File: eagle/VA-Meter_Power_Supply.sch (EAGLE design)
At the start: 18 parts, among them IC2 7805TV, T1 2SA1359

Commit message: Power Supply 回路図、基板図修正
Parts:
- JP1: device pinhead:PINHD-1X3 -> pinhead:PINHD-2X3
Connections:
- net 3.3V: now also JP1.3, JP1.4; no longer JP1.2
- net 5V: now also JP1.2
- net V-GND: now also JP1.5, JP1.6; no longer JP1.3
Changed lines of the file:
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@@
 <setting verticaltext="up"/>
 </settings>
-<grid distance="0.1" unitdist="inch" unit="inch" style="dots" multiple="1" display="yes" altdistance="0.01" altunitdist="inch" altunit="inch"/>
+<grid distance="0.1" unitdist="inch" unit="inch" style="lines" multiple="1" display="yes" altdistance="0.01" altunitdist="inch" altunit="inch"/>
 <layers>
 <layer number="1" name="Top" color="4" fill="1" visible="no" active="no"/>
@@
 <part name="PF1" library="polyswitch" deviceset="PTC-" device="PF-5.1"/>
 <part name="FRAME1" library="frames" deviceset="A4L-LOC" device=""/>
-<part name="JP1" library="pinhead" deviceset="PINHD-1X3" device=""/>
+<part name="JP1" library="pinhead" deviceset="PINHD-2X3" device=""/>
 </parts>
 <sheets>
@@
 <wire x1="121.92" y1="60.96" x2="137.16" y2="60.96" width="0.1524" layer="91"/>
 <label x="127" y="60.96" size="1.778" layer="95"/>
+<wire x1="121.92" y1="71.12" x2="149.86" y2="71.12" width="0.1524" layer="91"/>
+<wire x1="149.86" y1="71.12" x2="149.86" y2="60.96" width="0.1524" layer="91"/>
+<junction x="121.92" y="71.12"/>
+<pinref part="JP1" gate="A" pin="2"/>
+<wire x1="149.86" y1="60.96" x2="144.78" y2="60.96" width="0.1524" layer="91"/>
 </segment>
 </net>
@@
 <wire x1="111.76" y1="48.26" x2="111.76" y2="45.72" width="0.1524" layer="91"/>
 <wire x1="99.06" y1="45.72" x2="111.76" y2="45.72" width="0.1524" layer="91"/>
-<pinref part="JP1" gate="A" pin="3"/>
+<pinref part="JP1" gate="A" pin="5"/>
 <wire x1="137.16" y1="55.88" x2="121.92" y2="55.88" width="0.1524" layer="91"/>
 <wire x1="121.92" y1="55.88" x2="121.92" y2="45.72" width="0.1524" layer="91"/>
@@
 <junction x="111.76" y="45.72"/>
 <label x="127" y="53.34" size="1.778" layer="95"/>
+<wire x1="121.92" y1="45.72" x2="149.86" y2="45.72" width="0.1524" layer="91"/>
+<junction x="121.92" y="45.72"/>
+<wire x1="149.86" y1="45.72" x2="149.86" y2="55.88" width="0.1524" layer="91"/>
+<pinref part="JP1" gate="A" pin="6"/>
+<wire x1="149.86" y1="55.88" x2="144.78" y2="55.88" width="0.1524" layer="91"/>
 </segment>
 </net>
@@
 <wire x1="111.76" y1="60.96" x2="111.76" y2="58.42" width="0.1524" layer="91"/>
 <wire x1="111.76" y1="58.42" x2="111.76" y2="53.34" width="0.1524" layer="91"/>
-<wire x1="137.16" y1="58.42" x2="111.76" y2="58.42" width="0.1524" layer="91"/>
+<wire x1="137.16" y1="58.42" x2="129.54" y2="58.42" width="0.1524" layer="91"/>
 <junction x="111.76" y="58.42"/>
-<pinref part="JP1" gate="A" pin="2"/>
+<pinref part="JP1" gate="A" pin="3"/>
 <label x="127" y="58.42" size="1.778" layer="95"/>
-</segment>
-</net>
+<wire x1="129.54" y1="58.42" x2="111.76" y2="58.42" width="0.1524" layer="91"/>
+<wire x1="129.54" y1="58.42" x2="129.54" y2="48.26" width="0.1524" layer="91"/>
+<junction x="129.54" y="58.42"/>
+<wire x1="129.54" y1="48.26" x2="152.4" y2="48.26" width="0.1524" layer="91"/>
+<wire x1="152.4" y1="48.26" x2="152.4" y2="58.42" width="0.1524" layer="91"/>
+<pinref part="JP1" gate="A" pin="4"/>
+<wire x1="152.4" y1="58.42" x2="144.78" y2="58.42" width="0.1524" layer="91"/>
+</segment>
+</net>

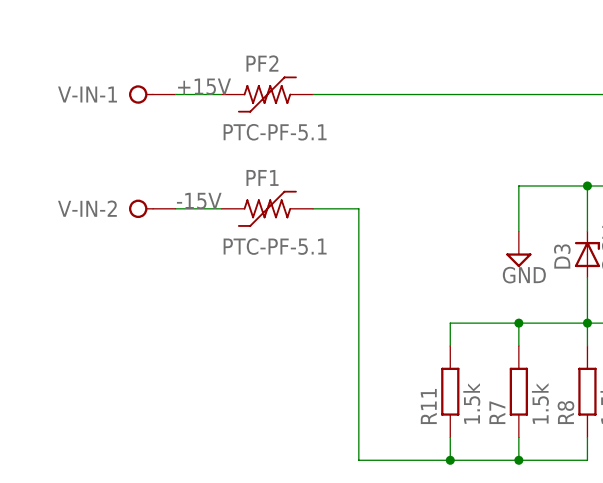
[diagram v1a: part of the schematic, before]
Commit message: VA-Meter_Power_Supply 測定部電源の回路図、基板図修正 入力端子にGNDを追加
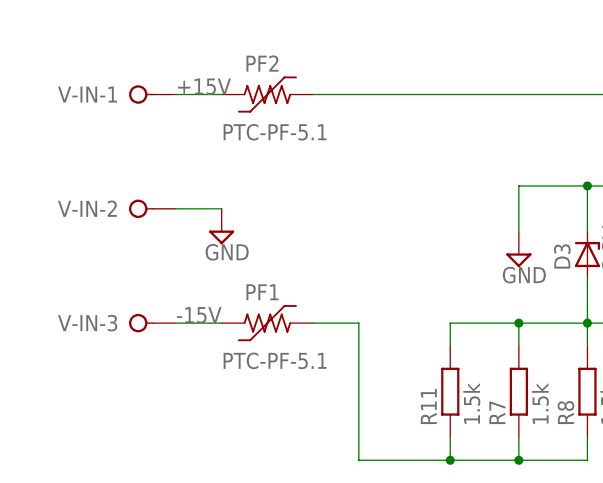
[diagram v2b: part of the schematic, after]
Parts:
- V-IN: device con-wago-508:W237-02P -> con-wago-508:W237-03P
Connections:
- net GND: now also V-IN-2.KL
- net N$7: now also V-IN-3.KL; no longer V-IN-2.KL
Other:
- moved on the sheet: PF1
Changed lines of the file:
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@@
 <setting verticaltext="up"/>
 </settings>
-<grid distance="0.1" unitdist="inch" unit="inch" style="lines" multiple="1" display="yes" altdistance="0.01" altunitdist="inch" altunit="inch"/>
+<grid distance="0.1" unitdist="inch" unit="inch" style="lines" multiple="1" display="no" altdistance="0.01" altunitdist="inch" altunit="inch"/>
 <layers>
 <layer number="1" name="Top" color="4" fill="1" visible="no" active="no"/>
@@
 <part name="C2" library="rcl" deviceset="CPOL-EU" device="E2.5-5" value="10u"/>
 <part name="C3" library="rcl" deviceset="CPOL-EU" device="E2.5-6" value="100u"/>
-<part name="V-IN" library="con-wago-508" deviceset="W237-02P" device=""/>
 <part name="D1" library="diode" deviceset="SCHOTTKY-DIODE" device="DO35-7" value="1S2"/>
 <part name="D2" library="diode" deviceset="ZENER-DIODE" device="ZD-5" value="3.6V"/>
@@
 <part name="FRAME1" library="frames" deviceset="A4L-LOC" device=""/>
 <part name="JP1" library="pinhead" deviceset="PINHD-2X3" device=""/>
+<part name="V-IN" library="con-wago-508" deviceset="W237-03P" device=""/>
+<part name="SUPPLY1" library="supply2" deviceset="GND" device=""/>
 </parts>
 <sheets>
@@
 <instance part="C2" gate="G$1" x="53.34" y="58.42"/>
 <instance part="C3" gate="G$1" x="99.06" y="58.42"/>
-<instance part="V-IN" gate="-1" x="-20.32" y="71.12"/>
-<instance part="V-IN" gate="-2" x="-20.32" y="58.42"/>
 <instance part="D1" gate="G$1" x="76.2" y="83.82" rot="R180"/>
 <instance part="D2" gate="G$1" x="111.76" y="50.8" rot="R90"/>
@@
 <instance part="R11" gate="G$1" x="15.24" y="38.1" rot="R90"/>
 <instance part="PF2" gate="G$1" x="-5.08" y="71.12"/>
-<instance part="PF1" gate="G$1" x="-5.08" y="58.42"/>
+<instance part="PF1" gate="G$1" x="-5.08" y="45.72"/>
 <instance part="FRAME1" gate="G$1" x="-55.88" y="-30.48"/>
 <instance part="JP1" gate="A" x="139.7" y="58.42"/>
+<instance part="V-IN" gate="-1" x="-20.32" y="71.12"/>
+<instance part="V-IN" gate="-2" x="-20.32" y="58.42"/>
+<instance part="V-IN" gate="-3" x="-20.32" y="45.72"/>
+<instance part="SUPPLY1" gate="GND" x="-10.16" y="55.88"/>
 </instances>
 <busses>
@@
 <wire x1="22.86" y1="60.96" x2="30.48" y2="60.96" width="0.1524" layer="91"/>
 <junction x="30.48" y="60.96"/>
+</segment>
+<segment>
+<pinref part="V-IN" gate="-2" pin="KL"/>
+<pinref part="SUPPLY1" gate="GND" pin="GND"/>
+<wire x1="-10.16" y1="58.42" x2="-15.24" y2="58.42" width="0.1524" layer="91"/>
 </segment>
 </net>
@@
 <net name="-15V" class="0">
 <segment>
-<label x="-15.24" y="58.42" size="1.778" layer="95"/>
+<label x="-15.24" y="45.72" size="1.778" layer="95"/>
 <pinref part="R8" gate="G$1" pin="1"/>
 <wire x1="30.48" y1="33.02" x2="30.48" y2="30.48" width="0.1524" layer="91"/>
@@
 <wire x1="15.24" y1="30.48" x2="5.08" y2="30.48" width="0.1524" layer="91"/>
 <junction x="15.24" y="30.48"/>
-<wire x1="5.08" y1="30.48" x2="5.08" y2="58.42" width="0.1524" layer="91"/>
+<wire x1="5.08" y1="30.48" x2="5.08" y2="45.72" width="0.1524" layer="91"/>
 <pinref part="PF1" gate="G$1" pin="2"/>
-<wire x1="0" y1="58.42" x2="5.08" y2="58.42" width="0.1524" layer="91"/>
+<wire x1="0" y1="45.72" x2="5.08" y2="45.72" width="0.1524" layer="91"/>
 </segment>
 </net>
@@
 <net name="N$6" class="0">
 <segment>
-<pinref part="V-IN" gate="-1" pin="KL"/>
 <pinref part="PF2" gate="G$1" pin="1"/>
 <wire x1="-15.24" y1="71.12" x2="-10.16" y2="71.12" width="0.1524" layer="91"/>
+<pinref part="V-IN" gate="-1" pin="KL"/>
 </segment>
 </net>
 <net name="N$7" class="0">
 <segment>
-<pinref part="V-IN" gate="-2" pin="KL"/>
 <pinref part="PF1" gate="G$1" pin="1"/>
-<wire x1="-15.24" y1="58.42" x2="-10.16" y2="58.42" width="0.1524" layer="91"/>
-</segment>
-</net>
+<wire x1="-15.24" y1="45.72" x2="-10.16" y2="45.72" width="0.1524" layer="91"/>
+<pinref part="V-IN" gate="-3" pin="KL"/>
+</segment>
+</net>

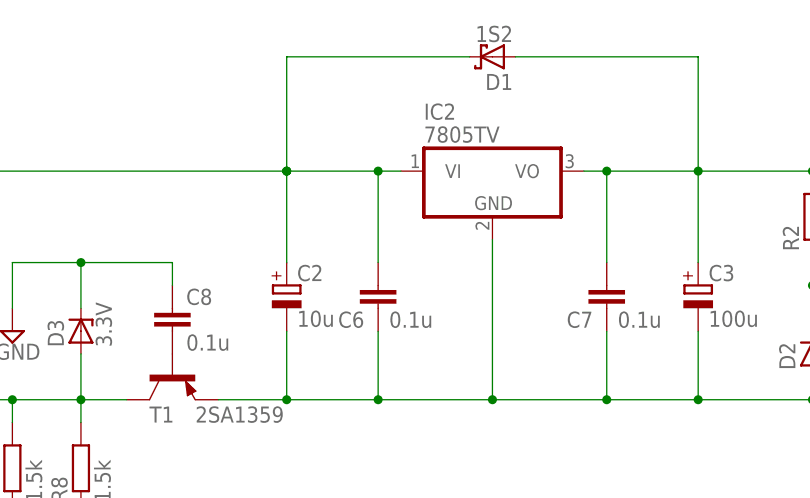
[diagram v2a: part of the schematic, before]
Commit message: VA-Meter_Power_Supply 回路図の電解コンデンサの値を47uFに変更
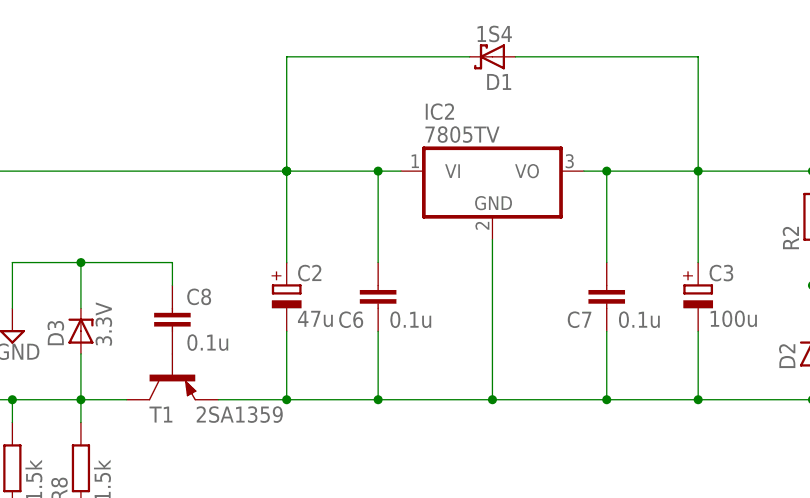
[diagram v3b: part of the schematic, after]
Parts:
- C2: value 10u -> 47u
- D1: value 1S2 -> 1S4
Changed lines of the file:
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@@
 <part name="R8" library="rcl" deviceset="R-EU_" device="0207/7" value="1.5k"/>
 <part name="SUPPLY4" library="supply2" deviceset="GND" device=""/>
-<part name="C2" library="rcl" deviceset="CPOL-EU" device="E2.5-5" value="10u"/>
+<part name="C2" library="rcl" deviceset="CPOL-EU" device="E2.5-5" value="47u"/>
 <part name="C3" library="rcl" deviceset="CPOL-EU" device="E2.5-6" value="100u"/>
-<part name="D1" library="diode" deviceset="SCHOTTKY-DIODE" device="DO35-7" value="1S2"/>
+<part name="D1" library="diode" deviceset="SCHOTTKY-DIODE" device="DO35-7" value="1S4"/>
 <part name="D2" library="diode" deviceset="ZENER-DIODE" device="ZD-5" value="3.6V"/>
 <part name="R2" library="rcl" deviceset="R-EU_" device="0204/7" value="220"/>

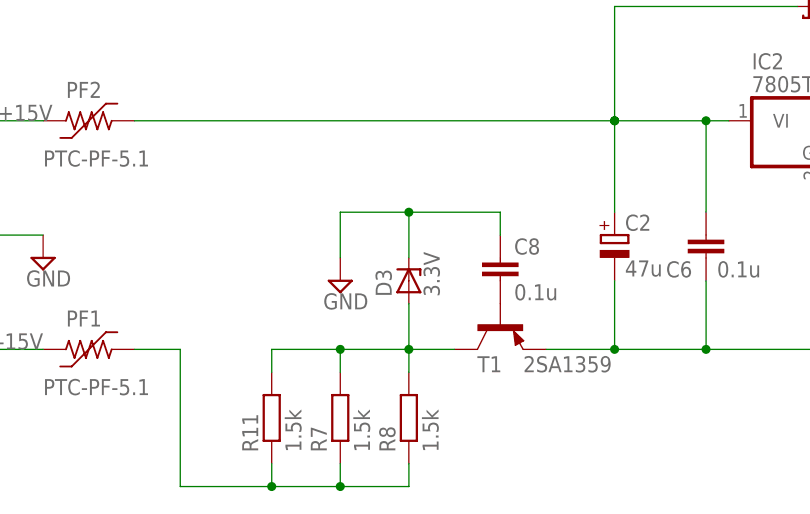
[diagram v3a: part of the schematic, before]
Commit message: VA-Meter_Power_Supply 2SA1359の定電圧源の回路が間違っていたので修正
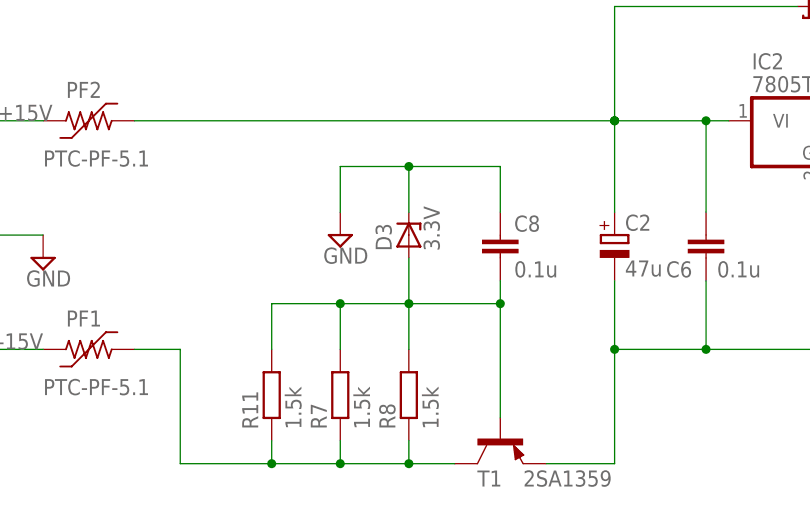
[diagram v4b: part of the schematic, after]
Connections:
- removed net N$1: D3.A, R11.2, R7.2, R8.2, T1.C
- removed net N$5: C8.2, T1.B
- new net N$2: C8.2, D3.A, R11.2, R7.2, R8.2, T1.B
- net -15V: now also T1.C
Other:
- moved on the sheet: C8, D3, R11, R7, R8, T1
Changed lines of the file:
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@@
 <instances>
 <instance part="IC2" gate="A1" x="76.2" y="71.12"/>
-<instance part="R8" gate="G$1" x="30.48" y="38.1" rot="R90"/>
-<instance part="SUPPLY4" gate="GND" x="22.86" y="53.34"/>
+<instance part="R8" gate="G$1" x="30.48" y="40.64" rot="R90"/>
+<instance part="SUPPLY4" gate="GND" x="22.86" y="58.42"/>
 <instance part="C2" gate="G$1" x="53.34" y="58.42"/>
 <instance part="C3" gate="G$1" x="99.06" y="58.42"/>
@@
 <attribute name="VALUE" x="94.996" y="55.499" size="1.778" layer="96" rot="R180"/>
 </instance>
-<instance part="D3" gate="G$1" x="30.48" y="53.34" rot="R90"/>
-<instance part="C8" gate="G$1" x="40.64" y="55.88"/>
-<instance part="T1" gate="G$1" x="40.64" y="48.26" smashed="yes" rot="R270">
-<attribute name="NAME" x="38.1" y="43.18" size="1.778" layer="95"/>
-<attribute name="VALUE" x="43.18" y="43.18" size="1.778" layer="96"/>
+<instance part="D3" gate="G$1" x="30.48" y="58.42" rot="R90"/>
+<instance part="C8" gate="G$1" x="40.64" y="58.42"/>
+<instance part="T1" gate="G$1" x="40.64" y="35.56" smashed="yes" rot="R270">
+<attribute name="NAME" x="38.1" y="30.48" size="1.778" layer="95"/>
+<attribute name="VALUE" x="43.18" y="30.48" size="1.778" layer="96"/>
 </instance>
-<instance part="R7" gate="G$1" x="22.86" y="38.1" rot="R90"/>
-<instance part="R11" gate="G$1" x="15.24" y="38.1" rot="R90"/>
+<instance part="R7" gate="G$1" x="22.86" y="40.64" rot="R90"/>
+<instance part="R11" gate="G$1" x="15.24" y="40.64" rot="R90"/>
 <instance part="PF2" gate="G$1" x="-5.08" y="71.12"/>
 <instance part="PF1" gate="G$1" x="-5.08" y="45.72"/>
@@
 <segment>
 <pinref part="SUPPLY4" gate="GND" pin="GND"/>
-<wire x1="22.86" y1="55.88" x2="22.86" y2="60.96" width="0.1524" layer="91"/>
+<wire x1="22.86" y1="60.96" x2="22.86" y2="66.04" width="0.1524" layer="91"/>
 <pinref part="D3" gate="G$1" pin="C"/>
-<wire x1="30.48" y1="60.96" x2="30.48" y2="55.88" width="0.1524" layer="91"/>
-<wire x1="30.48" y1="60.96" x2="40.64" y2="60.96" width="0.1524" layer="91"/>
+<wire x1="30.48" y1="66.04" x2="30.48" y2="60.96" width="0.1524" layer="91"/>
+<wire x1="30.48" y1="66.04" x2="40.64" y2="66.04" width="0.1524" layer="91"/>
 <pinref part="C8" gate="G$1" pin="1"/>
-<wire x1="40.64" y1="60.96" x2="40.64" y2="58.42" width="0.1524" layer="91"/>
-<wire x1="22.86" y1="60.96" x2="30.48" y2="60.96" width="0.1524" layer="91"/>
-<junction x="30.48" y="60.96"/>
+<wire x1="40.64" y1="66.04" x2="40.64" y2="60.96" width="0.1524" layer="91"/>
+<wire x1="22.86" y1="66.04" x2="30.48" y2="66.04" width="0.1524" layer="91"/>
+<junction x="30.48" y="66.04"/>
 </segment>
 <segment>
@@
 <label x="-15.24" y="45.72" size="1.778" layer="95"/>
 <pinref part="R8" gate="G$1" pin="1"/>
-<wire x1="30.48" y1="33.02" x2="30.48" y2="30.48" width="0.1524" layer="91"/>
+<wire x1="30.48" y1="35.56" x2="30.48" y2="33.02" width="0.1524" layer="91"/>
 <pinref part="R11" gate="G$1" pin="1"/>
-<wire x1="15.24" y1="33.02" x2="15.24" y2="30.48" width="0.1524" layer="91"/>
-<wire x1="15.24" y1="30.48" x2="22.86" y2="30.48" width="0.1524" layer="91"/>
+<wire x1="15.24" y1="35.56" x2="15.24" y2="33.02" width="0.1524" layer="91"/>
+<wire x1="15.24" y1="33.02" x2="22.86" y2="33.02" width="0.1524" layer="91"/>
 <pinref part="R7" gate="G$1" pin="1"/>
-<wire x1="22.86" y1="30.48" x2="30.48" y2="30.48" width="0.1524" layer="91"/>
-<wire x1="22.86" y1="33.02" x2="22.86" y2="30.48" width="0.1524" layer="91"/>
-<junction x="22.86" y="30.48"/>
-<wire x1="15.24" y1="30.48" x2="5.08" y2="30.48" width="0.1524" layer="91"/>
-<junction x="15.24" y="30.48"/>
-<wire x1="5.08" y1="30.48" x2="5.08" y2="45.72" width="0.1524" layer="91"/>
+<wire x1="22.86" y1="33.02" x2="30.48" y2="33.02" width="0.1524" layer="91"/>
+<wire x1="22.86" y1="35.56" x2="22.86" y2="33.02" width="0.1524" layer="91"/>
+<junction x="22.86" y="33.02"/>
+<wire x1="15.24" y1="33.02" x2="5.08" y2="33.02" width="0.1524" layer="91"/>
+<junction x="15.24" y="33.02"/>
+<wire x1="5.08" y1="33.02" x2="5.08" y2="45.72" width="0.1524" layer="91"/>
 <pinref part="PF1" gate="G$1" pin="2"/>
 <wire x1="0" y1="45.72" x2="5.08" y2="45.72" width="0.1524" layer="91"/>
-</segment>
-</net>
-<net name="N$1" class="0">
-<segment>
-<pinref part="R8" gate="G$1" pin="2"/>
-<pinref part="D3" gate="G$1" pin="A"/>
-<wire x1="30.48" y1="50.8" x2="30.48" y2="45.72" width="0.1524" layer="91"/>
+<wire x1="30.48" y1="33.02" x2="35.56" y2="33.02" width="0.1524" layer="91"/>
+<junction x="30.48" y="33.02"/>
 <pinref part="T1" gate="G$1" pin="C"/>
-<wire x1="30.48" y1="45.72" x2="30.48" y2="43.18" width="0.1524" layer="91"/>
-<wire x1="35.56" y1="45.72" x2="30.48" y2="45.72" width="0.1524" layer="91"/>
-<junction x="30.48" y="45.72"/>
-<wire x1="30.48" y1="45.72" x2="22.86" y2="45.72" width="0.1524" layer="91"/>
-<pinref part="R11" gate="G$1" pin="2"/>
-<wire x1="22.86" y1="45.72" x2="15.24" y2="45.72" width="0.1524" layer="91"/>
-<wire x1="15.24" y1="45.72" x2="15.24" y2="43.18" width="0.1524" layer="91"/>
-<pinref part="R7" gate="G$1" pin="2"/>
-<wire x1="22.86" y1="43.18" x2="22.86" y2="45.72" width="0.1524" layer="91"/>
-<junction x="22.86" y="45.72"/>
-</segment>
-</net>
-<net name="N$5" class="0">
-<segment>
-<pinref part="T1" gate="G$1" pin="B"/>
-<pinref part="C8" gate="G$1" pin="2"/>
 </segment>
 </net>
@@
 <wire x1="88.9" y1="53.34" x2="88.9" y2="45.72" width="0.1524" layer="91"/>
 <junction x="88.9" y="45.72"/>
-<pinref part="T1" gate="G$1" pin="E"/>
-<wire x1="45.72" y1="45.72" x2="53.34" y2="45.72" width="0.1524" layer="91"/>
-<junction x="53.34" y="45.72"/>
 <pinref part="D2" gate="G$1" pin="A"/>
 <wire x1="111.76" y1="48.26" x2="111.76" y2="45.72" width="0.1524" layer="91"/>
@@
 <pinref part="JP1" gate="A" pin="6"/>
 <wire x1="149.86" y1="55.88" x2="144.78" y2="55.88" width="0.1524" layer="91"/>
+<pinref part="T1" gate="G$1" pin="E"/>
+<wire x1="53.34" y1="33.02" x2="45.72" y2="33.02" width="0.1524" layer="91"/>
+<wire x1="53.34" y1="33.02" x2="53.34" y2="45.72" width="0.1524" layer="91"/>
+<junction x="53.34" y="45.72"/>
 </segment>
 </net>
@@
 </segment>
 </net>
+<net name="N$2" class="0">
+<segment>
+<pinref part="R7" gate="G$1" pin="2"/>
+<pinref part="R8" gate="G$1" pin="2"/>
+<pinref part="D3" gate="G$1" pin="A"/>
+<wire x1="30.48" y1="55.88" x2="30.48" y2="50.8" width="0.1524" layer="91"/>
+<wire x1="30.48" y1="50.8" x2="30.48" y2="45.72" width="0.1524" layer="91"/>
+<pinref part="T1" gate="G$1" pin="B"/>
+<pinref part="C8" gate="G$1" pin="2"/>
+<wire x1="40.64" y1="53.34" x2="40.64" y2="50.8" width="0.1524" layer="91"/>
+<wire x1="40.64" y1="50.8" x2="40.64" y2="38.1" width="0.1524" layer="91"/>
+<wire x1="30.48" y1="50.8" x2="40.64" y2="50.8" width="0.1524" layer="91"/>
+<junction x="30.48" y="50.8"/>
+<junction x="40.64" y="50.8"/>
+<wire x1="30.48" y1="50.8" x2="22.86" y2="50.8" width="0.1524" layer="91"/>
+<pinref part="R11" gate="G$1" pin="2"/>
+<wire x1="22.86" y1="50.8" x2="15.24" y2="50.8" width="0.1524" layer="91"/>
+<wire x1="15.24" y1="50.8" x2="15.24" y2="45.72" width="0.1524" layer="91"/>
+<wire x1="22.86" y1="45.72" x2="22.86" y2="50.8" width="0.1524" layer="91"/>
+<junction x="22.86" y="50.8"/>
+</segment>
+</net>
